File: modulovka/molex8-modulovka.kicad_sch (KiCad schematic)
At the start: 7 parts, among them J1 2xMVE252-5-V, J2 TME 39281083 MOLEX, J3 2xMVE252-5-V

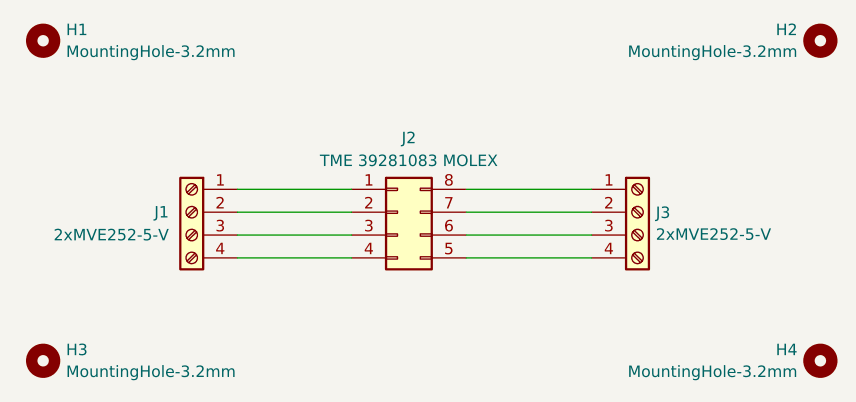
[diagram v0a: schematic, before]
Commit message: modulovka: name wires, fix conn symbol, fix switched 2-3.
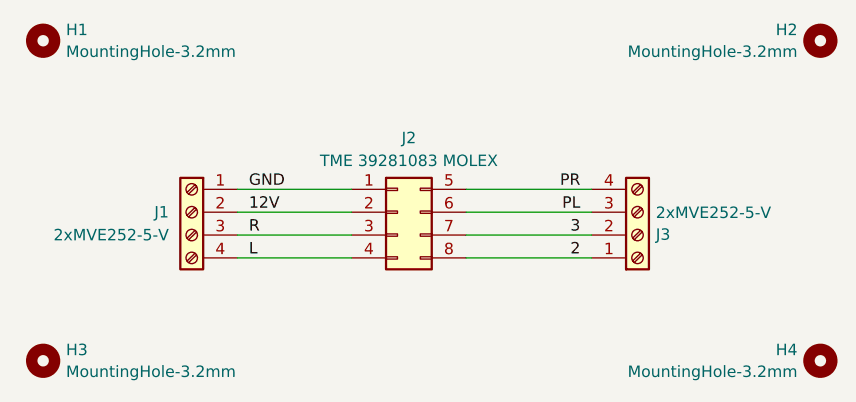
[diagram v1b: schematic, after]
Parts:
- J2: symbol Connector_Generic:Conn_02x04_Counter_Clockwise -> Connector_Generic:Conn_02x04_Top_Bottom
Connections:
- net GND: now reaches J1.1 (Pin_1), J2.1 (Pin_1)
- net 12V: now reaches J1.2 (Pin_2), J2.2 (Pin_2)
- net R: now reaches J1.3 (Pin_3), J2.3 (Pin_3)
- net L: now reaches J1.4 (Pin_4), J2.4 (Pin_4)
- net PR: now reaches J2.5 (Pin_5), J3.4 (Pin_4)
- net PL: now reaches J2.6 (Pin_6), J3.3 (Pin_3)
- net 3: now reaches J2.7 (Pin_7), J3.2 (Pin_2)
- net 2: now reaches J2.8 (Pin_8), J3.1 (Pin_1)
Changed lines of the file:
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@@
 	(title_block
 		(title "MOLEX to screw-terminals PCB for modules connection")
-		(date "2022-12-02")
-		(rev "1.0")
+		(date "2025-05-13")
+		(rev "1.2")
 		(comment 4 "Silkscreen texts added compared to plain molex8 pcb.")
 	)
@@
 		)
 	)
+	(label "2"
+		(at 119.38 64.77 180)
+		(effects
+			(font
+				(size 1.27 1.27)
+			)
+			(justify right bottom)
+		)
+	)
+	(label "12V"
+		(at 82.55 59.69 0)
+		(effects
+			(font
+				(size 1.27 1.27)
+			)
+			(justify left bottom)
+		)
+	)
+	(label "PL"
+		(at 119.38 59.69 180)
+		(effects
+			(font
+				(size 1.27 1.27)
+			)
+			(justify right bottom)
+		)
+	)
+	(label "L"
+		(at 82.55 64.77 0)
+		(effects
+			(font
+				(size 1.27 1.27)
+			)
+			(justify left bottom)
+		)
+	)
+	(label "3"
+		(at 119.38 62.23 180)
+		(effects
+			(font
+				(size 1.27 1.27)
+			)
+			(justify right bottom)
+		)
+	)
+	(label "R"
+		(at 82.55 62.23 0)
+		(effects
+			(font
+				(size 1.27 1.27)
+			)
+			(justify left bottom)
+		)
+	)
+	(label "PR"
+		(at 119.38 57.15 180)
+		(effects
+			(font
+				(size 1.27 1.27)
+			)
+			(justify right bottom)
+		)
+	)
+	(label "GND"
+		(at 82.55 57.15 0)
+		(effects
+			(font
+				(size 1.27 1.27)
+			)
+			(justify left bottom)
+		)
+	)
 	(symbol
-		(lib_id "Connector_Generic:Conn_02x04_Counter_Clockwise")
+		(lib_id "Connector_Generic:Conn_02x04_Top_Bottom")
 		(at 99.06 59.69 0)
 		(unit 1)
@@
 			)
 		)
-		(property "Description" ""
+		(property "Description" "Generic connector, double row, 02x04, top/bottom pin numbering scheme (row 1: 1...pins_per_row, row2: pins_per_row+1 ... num_pins), script generated (kicad-library-utils/schlib/autogen/connector/)"
 			(at 99.06 59.69 0)
 			(effects
@@
 					(size 1.27 1.27)
 				)
+				(hide yes)
 			)
 		)
@@
 	(symbol
 		(lib_id "Connector:Screw_Terminal_01x04")
-		(at 125.73 59.69 0)
+		(at 125.73 62.23 0)
+		(mirror x)
 		(unit 1)
 		(exclude_from_sim no)
@@
 		(on_board yes)
 		(dnp no)
-		(fields_autoplaced yes)
 		(property "Reference" "J3"
+			(at 127.762 62.1721 0)
+			(effects
+				(font
+					(size 1.27 1.27)
+				)
+				(justify left)
+			)
+		)
+		(property "Value" "2xMVE252-5-V"
 			(at 127.762 59.7479 0)
 			(effects
@@
 			)
 		)
-		(property "Value" "2xMVE252-5-V"
-			(at 127.762 62.1721 0)
-			(effects
-				(font
-					(size 1.27 1.27)
-				)
-				(justify left)
-			)
-		)
 		(property "Footprint" "TerminalBlock_Euroclamp:MVE252-5-V-2x"
-			(at 125.73 59.69 0)
+			(at 125.73 62.23 0)
 			(effects
 				(font
@@
 		)
 		(property "Datasheet" "~"
-			(at 125.73 59.69 0)
+			(at 125.73 62.23 0)
 			(effects
 				(font
@@
 		)
 		(property "Description" ""
-			(at 125.73 59.69 0)
-			(effects
-				(font
+			(at 125.73 62.23 0)
+			(effects
+				(font
